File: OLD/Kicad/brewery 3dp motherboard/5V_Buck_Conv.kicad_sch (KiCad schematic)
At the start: 31 parts, among them U4 LM25145RGYR, U7 DOZ45N03T, U8 DOZ45N03T

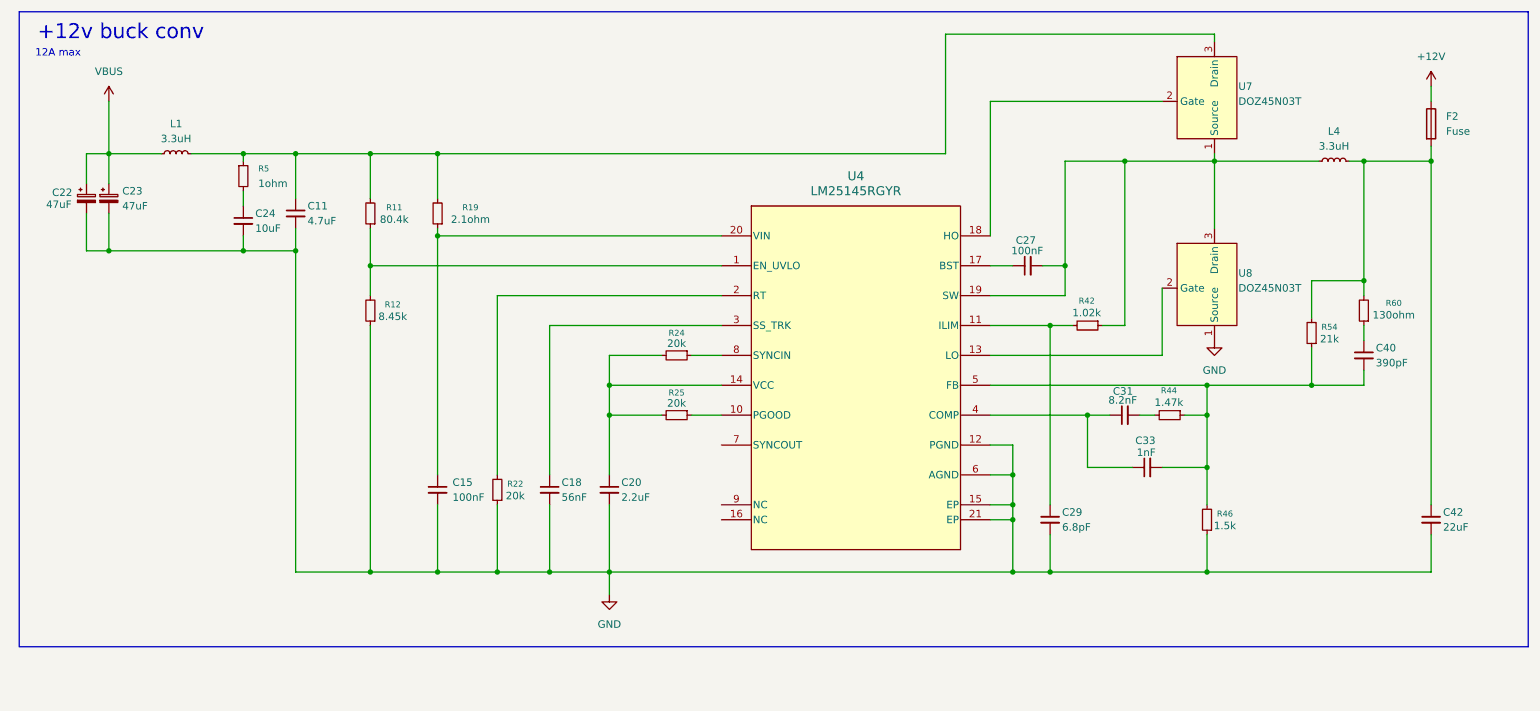
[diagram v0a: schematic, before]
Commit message: cleaned up structure a bit
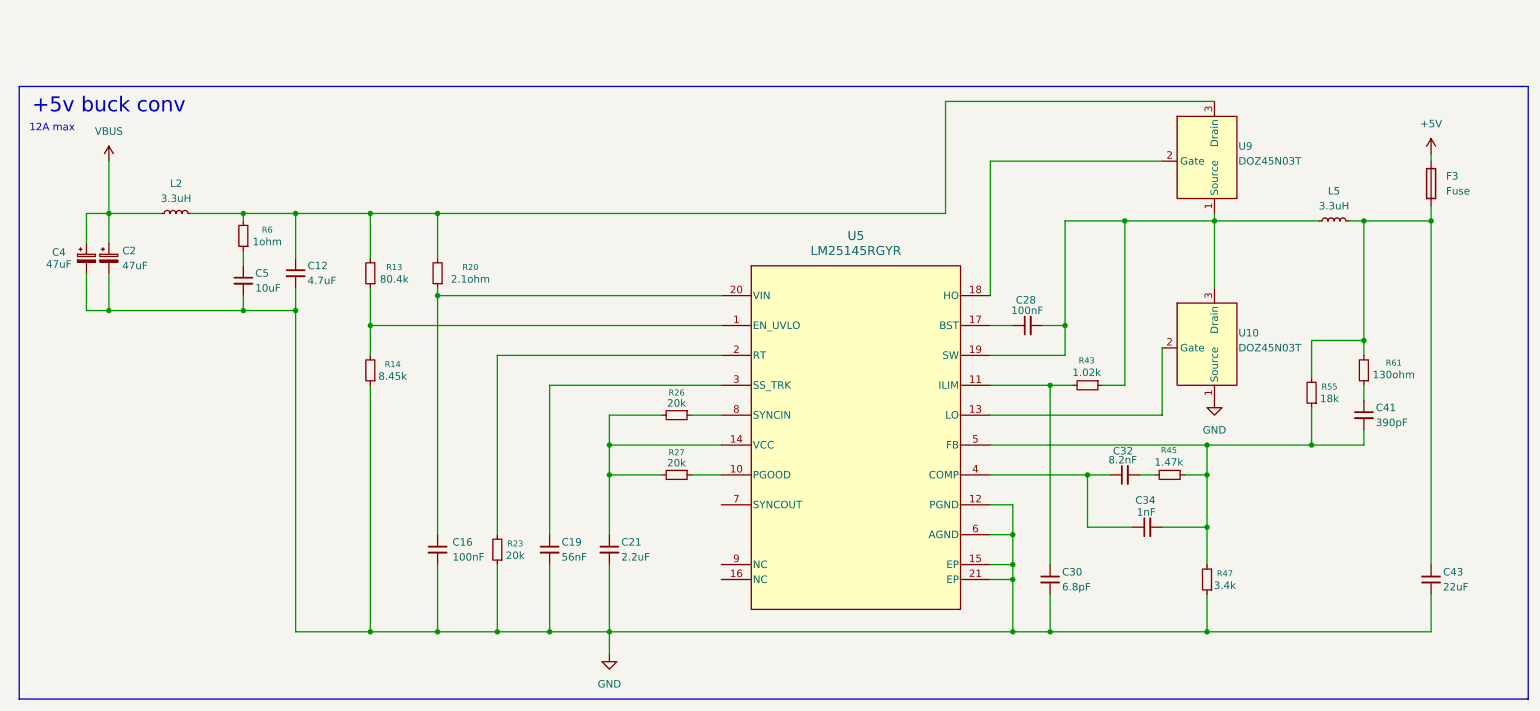
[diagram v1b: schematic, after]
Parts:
- removed C11: 4.7uF, Capacitor_SMD:C_1210_3225Metric, symbol Device:C_Small
- removed C15: 100nF, Capacitor_SMD:C_0402_1005Metric, symbol Device:C_Small
- removed C18: 56nF, Capacitor_SMD:C_0402_1005Metric, symbol Device:C_Small
- removed C20: 2.2uF, Capacitor_SMD:C_1206_3216Metric, symbol Device:C_Small
- removed C22, C23: 47uF, Capacitor_THT:C_Radial_D6.3mm_H7.0mm_P2.50mm, symbol Device:C_Polarized_Small
- removed C24: 10uF, Capacitor_SMD:C_1210_3225Metric, symbol Device:C_Small
- removed C27: 100nF, Capacitor_SMD:C_0603_1608Metric, symbol Device:C_Small
- removed C29: 6.8pF, Capacitor_SMD:C_0603_1608Metric, symbol Device:C_Small
- removed C31: 8.2nF, Capacitor_SMD:C_0402_1005Metric, symbol Device:C_Small
- removed C33: 1nF, Capacitor_SMD:C_0402_1005Metric, symbol Device:C_Small
- removed C40: 390pF, Capacitor_SMD:C_0402_1005Metric, symbol Device:C_Small
- removed C42: 22uF, Capacitor_SMD:C_1210_3225Metric, symbol Device:C_Small
- removed F2: Fuse, footprints:XF-509P, symbol Device:Fuse
- removed L1, L4: 3.3uH, footprints:IND_SRP1038A_BRN-M, symbol Device:L_Small
- removed R11: 80.4k, Resistor_SMD:R_0402_1005Metric, symbol Device:R_Small
- removed R12: 8.45k, Resistor_SMD:R_0402_1005Metric, symbol Device:R_Small
- removed R19: 2.1ohm, Resistor_SMD:R_0402_1005Metric, symbol Device:R_Small
- removed R22, R24, R25: 20k, Resistor_SMD:R_0402_1005Metric, symbol Device:R_Small
- removed R42: 1.02k, Resistor_SMD:R_0603_1608Metric, symbol Device:R_Small
- removed R44: 1.47k, Resistor_SMD:R_0402_1005Metric, symbol Device:R_Small
- removed R46: 1.5k, Resistor_SMD:R_0402_1005Metric, symbol Device:R_Small
- removed R5: 1ohm, Resistor_SMD:R_0603_1608Metric, symbol Device:R_Small
- removed R54: 21k, Resistor_SMD:R_0402_1005Metric, symbol Device:R_Small
- removed R60: 130ohm, Resistor_SMD:R_0402_1005Metric, symbol Device:R_Small
- removed U4: LM25145RGYR, footprints:RGY0020B, symbol symbols:LM25145RGYR
- removed U7, U8: DOZ45N03T, DOZ45N03T:DOZ45N03T, symbol DOZ45N03T:DOZ45N03T
- added C12: 4.7uF, Capacitor_SMD:C_0603_1608Metric, symbol Device:C_Small
- added C16, C28: 100nF, Capacitor_SMD:C_0402_1005Metric, symbol Device:C_Small
- added C19: 56nF, Capacitor_SMD:C_0402_1005Metric, symbol Device:C_Small
- added C2, C4: 47uF, Capacitor_THT:C_Radial_D6.3mm_H7.0mm_P2.50mm, symbol Device:C_Polarized_Small
- added C21: 2.2uF, Capacitor_SMD:C_1206_3216Metric, symbol Device:C_Small
- added C30: 6.8pF, Capacitor_SMD:C_0402_1005Metric, symbol Device:C_Small
- added C32: 8.2nF, Capacitor_SMD:C_0402_1005Metric, symbol Device:C_Small
- added C34: 1nF, Capacitor_SMD:C_0402_1005Metric, symbol Device:C_Small
- added C41: 390pF, Capacitor_SMD:C_0402_1005Metric, symbol Device:C_Small
- added C43: 22uF, Capacitor_SMD:C_1210_3225Metric, symbol Device:C_Small
- added C5: 10uF, Capacitor_SMD:C_1210_3225Metric, symbol Device:C_Small
- added F3: Fuse, footprints:XF-509P, symbol Device:Fuse
- added L2, L5: 3.3uH, footprints:IND_SRP1038A_BRN-M, symbol Device:L_Small
- added R13: 80.4k, Resistor_SMD:R_0402_1005Metric, symbol Device:R_Small
- added R14: 8.45k, Resistor_SMD:R_0402_1005Metric, symbol Device:R_Small
- added R20: 2.1ohm, Resistor_SMD:R_0402_1005Metric, symbol Device:R_Small
- added R23, R26, R27: 20k, Resistor_SMD:R_0402_1005Metric, symbol Device:R_Small
- added R43: 1.02k, Resistor_SMD:R_0402_1005Metric, symbol Device:R_Small
- added R45: 1.47k, Resistor_SMD:R_0402_1005Metric, symbol Device:R_Small
- added R47: 3.4k, Resistor_SMD:R_0402_1005Metric, symbol Device:R_Small
- added R55: 18k, Resistor_SMD:R_0402_1005Metric, symbol Device:R_Small
- added R6: 1ohm, Resistor_SMD:R_0603_1608Metric, symbol Device:R_Small
- added R61: 130ohm, Resistor_SMD:R_0402_1005Metric, symbol Device:R_Small
- added U10, U9: DOZ45N03T, DOZ45N03T:DOZ45N03T, symbol DOZ45N03T:DOZ45N03T
- added U5: LM25145RGYR, footprints:RGY0020B, symbol symbols:LM25145RGYR
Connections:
- net GND: now also C12.2, C16.2, C19.2, C2.2, C21.2, C30.2, C4.2, C43.2, C5.2, R14.1, R23.1, R47.1, U10.1 (Source), U5.12 (PGND), U5.15 (EP), U5.21 (EP), U5.6 (AGND)
- net VBUS: now also C2.1, C4.1, L2.1
- new net: C16.1, R20.1, U5.20 (VIN)
- new net: C32.1, C34.1, U5.4 (COMP)
- new net: C32.2, R45.2
- new net: R13.1, R14.2, U5.1 (EN_UVLO)
- new net: C12.1, L2.2, R13.2, R20.2, R6.2, U9.3 (Drain)
- new net: C41.1, R61.1
- new net: C34.2, C41.2, R45.1, R47.2, R55.1, U5.5 (FB)
- new net: C19.1, U5.3 (SS_TRK)
- new net: R27.1, U5.10 (PGOOD)
- new net: C30.1, R43.2, U5.11 (ILIM)
- new net: U10.2 (Gate), U5.13 (LO)
- new net: C21.1, R26.2, R27.2, U5.14 (VCC)
- new net: C28.1, U5.17 (BST)
- new net: U5.18 (HO), U9.2 (Gate)
- new net: C28.2, L5.1, R43.1, U10.3 (Drain), U5.19 (SW), U9.1 (Source)
- new net: R23.2, U5.2 (RT)
- new net: R26.1, U5.8 (SYNCIN)
- new net: C43.1, F3.2, L5.2, R55.2, R61.2
- new net: C5.1, R6.1
- new net +5V: F3.1
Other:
- note added: "+5v buck conv"
- note removed: "+12v buck conv"
